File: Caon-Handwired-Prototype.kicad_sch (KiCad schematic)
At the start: 0 parts

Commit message: s
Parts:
- added S_C1: 0.1uF, Caon65:Capacitor_0805, symbol Device:C_Small
- added S_D1, S_D2, S_D3, S_D4, S_D5, S_D6, S_D7, S_D8: 1N4148, Caon65:D_SOD-123_1N4148W, symbol Caon65:Diode_1N4148W_SOD-123
- added U1: 74HC595, Caon65:74HC595A, symbol 74xx:74HC595
- added U2: Nice!Nano/SuperMini nRF52840, Caon65:SuperMini_NiceNano_USBdn, symbol Caon65:SuperMini/NiceNano_nRF52840
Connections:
- new net: S_D5.8 (A), U1.4 (QE)
- new net: S_D1.8 (A), U1.15 (QA)
- new net: S_D3.8 (A), U1.2 (QC)
- new net: S_D7.8 (A), U1.6 (QG)
- new net: S_D2.8 (A), U1.1 (QB)
- new net: S_D4.8 (A), U1.3 (QD)
- new net: S_D6.8 (A), U1.5 (QF)
- new net: S_D8.8 (A), U1.7 (QH)
- new net +3V3: S_C1.1, U1.10 (~{SRCLR}), U1.16 (VCC)
- new net CS: U1.12 (RCLK), U2.017 (P0.17)
- new net ENC1_A: U2.104 (P1.04-LF)
- new net ENC1_B: U2.106 (P1.06-LF)
- new net ENC2_A: U2.010 (P0.10-LF)
- new net ENC2_B: U2.009 (P0.09-LF)
- new net GND: S_C1.2, U1.13 (~{OE}), U1.8 (GND), U2.B- (BAT-), U2.GD (GND)
- new net MOSI: U1.14 (SER), U2.006 (P0.06)
- new net QH': U1.9 (QH')
- new net Row 0: U2.031 (P0.31-LF)
- new net Row 1: U2.029 (P0.29-LF)
- new net SCK: U1.11 (SRCLK), U2.008 (P0.08)
- new net VCC: U2.3V3
- new net col 0: S_D1.7 (K)
- new net col 1: S_D2.7 (K)
- new net col 2: S_D3.7 (K)
- new net col 3: S_D4.7 (K)
- new net col 4: S_D5.7 (K)
- new net col 5: S_D6.7 (K)
- new net col 6: S_D7.7 (K)
- new net col 7: S_D8.7 (K)
- no-connect marks 0 -> 15
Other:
- note added: "Nice!Nano/Super Mini"
- note added: "Shifter"

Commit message: Schematic Update
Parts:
- removed U2: Nice!Nano/SuperMini nRF52840, Caon65:SuperMini_NiceNano_USBdn, symbol Caon65:SuperMini/NiceNano_nRF52840
- added U2: SuperMini nRF52840, PCM_marbastlib-xp-promicroish:SuperMini_nRF52840_AH_USBup, symbol PCM_marbastlib-promicroish:SuperMini_nRF52840
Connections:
- net CS: now also U2.5 (P0.17)
- net ENC1_A: now also U2.11 (P1.04-LF)
- net ENC1_B: now also U2.12 (P1.06-LF)
- net ENC2_A: now also U2.23 (P0.10-LF)
- net ENC2_B: now also U2.24 (P0.09-LF)
- net GND: now also U2.14 (GND), U2.28 (GND), U2.3 (GND), U2.4 (GND)
- net MOSI: now also U2.1 (P0.06)
- net Row 0: now also U2.17 (P0.31-LF)
- net Row 1: now also U2.18 (P0.29-LF)
- net SCK: now also U2.2 (P0.08)
- net VCC: now also U2.16 (3V3)
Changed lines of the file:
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@@
-	)
-	(symbol
-		(lib_id "Caon65:SuperMini/NiceNano_nRF52840")
-		(at 63.5 50.8 0)
-		(unit 1)
-		(exclude_from_sim no)
-		(in_bom no)
-		(on_board yes)
-		(dnp no)
-		(fields_autoplaced yes)
-		(property "Reference" "U2"
-			(at 63.5 27.94 0)
-			(effects
-				(font
-					(size 1.27 1.27)
-				)
-				(hide yes)
-			)
-		)
-		(property "Value" "Nice!Nano/SuperMini nRF52840"
-			(at 63.5 29.21 0)
-			(effects
-				(font
-					(size 1.27 1.27)
-				)
-			)
-		)
-		(property "Footprint" "Caon65:SuperMini_NiceNano_USBdn"
-			(at 63.5 81.28 0)
-			(effects
-				(font
-					(size 1.27 1.27)
-				)
-				(hide yes)
-			)
-		)
-		(property "Datasheet" "https://wiki.icbbuy.com/doku.php?id=developmentboard:nrf52840"
-			(at 64.77 83.82 0)
-			(effects
-				(font
-					(size 1.27 1.27)
-				)
-				(hide yes)
-			)
-		)
-		(property "Description" "Symbol for an nicekeyboards nice!nano"
-			(at 63.5 50.8 0)
-			(effects
-				(font
-					(size 1.27 1.27)
-				)
-				(hide yes)
-			)
-		)
-		(property "Datasheet2" "https://nicekeyboards.com/docs/nice-nano/pinout-schematic"
-			(at 63.754 86.106 0)
-			(effects
-				(font
-					(size 1.27 1.27)
-				)
-				(hide yes)
-			)
-		)
-		(pin "006"
-		)
-		(pin "102"
-		)
-		(pin "106"
-		)
-		(pin "002"
-		)
-		(pin "017"
-		)
-		(pin "010"
-		)
-		(pin "GD"
-		)
-		(pin "RS"
-		)
-		(pin "008"
-		)
-		(pin "029"
-		)
-		(pin "022"
-		)
-		(pin "107"
-		)
-		(pin "009"
-		)
-		(pin "113"
-		)
-		(pin "100"
-		)
-		(pin "B+"
-		)
-		(pin "020"
-		)
-		(pin "104"
-		)
-		(pin "031"
-		)
-		(pin "101"
-		)
-		(pin "3V3"
-		)
-		(pin "024"
-		)
-		(pin "111"
-		)
-		(pin "115"
-		)
-		(pin "011"
-		)
-		(pin "B+"
-		)
-		(pin "B-"
-		)
-		(pin "GD"
-		)
-		(pin "GD"
-		)
-		(instances
-			(project "Caon-Handwired-Prototype"
-				(path "/8df2f29a-df03-4271-980f-9b5acafffeb5"
-					(reference "U2")
-					(unit 1)
-				)
-			)
-		)
 	)
 	(symbol
@@
 		(on_board yes)
 		(dnp no)
-		(property "Reference" "#PWR03"
+		(property "Reference" "#PWR02"
 			(at 95.25 46.99 0)
 			(effects
@@
 			(project "Caon-Handwired-Prototype"
 				(path "/8df2f29a-df03-4271-980f-9b5acafffeb5"
-					(reference "#PWR03")
+					(reference "#PWR02")
 					(unit 1)
 				)
@@
 		(on_board yes)
 		(dnp no)
-		(property "Reference" "#PWR04"
+		(property "Reference" "#PWR03"
 			(at 34.29 49.53 0)
 			(effects
@@
 			(project "Caon-Handwired-Prototype"
 				(path "/8df2f29a-df03-4271-980f-9b5acafffeb5"
-					(reference "#PWR04")
+					(reference "#PWR03")
 					(unit 1)
 				)
@@
 		(on_board yes)
 		(dnp no)
-		(property "Reference" "#PWR06"
+		(property "Reference" "#PWR04"
 			(at 129.54 74.93 0)
 			(effects
@@
 			(project "Caon-Handwired-Prototype"
 				(path "/8df2f29a-df03-4271-980f-9b5acafffeb5"
-					(reference "#PWR06")
-					(unit 1)
-				)
+					(reference "#PWR04")
+					(unit 1)
+				)
+			)
+		)
+	)
+	(symbol
+		(lib_id "PCM_marbastlib-promicroish:SuperMini_nRF52840")
+		(at 63.5 50.8 0)
+		(unit 1)
+		(exclude_from_sim no)
+		(in_bom no)
+		(on_board yes)
+		(dnp no)
+		(fields_autoplaced yes)
+		(property "Reference" "U2"
+			(at 63.5 26.67 0)
+			(effects
+				(font
+					(size 1.27 1.27)
+				)
+			)
+		)
+		(property "Value" "SuperMini nRF52840"
+			(at 63.5 29.21 0)
+			(effects
+				(font
+					(size 1.27 1.27)
+				)
+			)
+		)
+		(property "Footprint" "PCM_marbastlib-xp-promicroish:SuperMini_nRF52840_AH_USBup"
+			(at 63.5 81.28 0)
+			(effects
+				(font
+					(size 1.27 1.27)
+				)
+				(hide yes)
+			)
+		)
+		(property "Datasheet" "https://wiki.icbbuy.com/doku.php?id=developmentboard:nrf52840"
+			(at 64.77 83.82 0)
+			(effects
+				(font
+					(size 1.27 1.27)
+				)
+				(hide yes)
+			)
+		)
+		(property "Description" "Symbol for an nicekeyboards nice!nano"
+			(at 63.5 50.8 0)
+			(effects
+				(font
+					(size 1.27 1.27)
+				)
+				(hide yes)
+			)
+		)
+		(pin "3"
+		)
+		(pin "11"
+		)
+		(pin "15"
+		)
+		(pin "18"
+		)
+		(pin "19"
+		)
+		(pin "1"
+		)
+		(pin "2"
+		)
+		(pin "6"
+		)
+		(pin "5"
+		)
+		(pin "8"
+		)
+		(pin "7"
+		)
+		(pin "14"
+		)
+		(pin "17"
+		)
+		(pin "4"
+		)
+		(pin "9"
+		)
+		(pin "10"
+		)
+		(pin "12"
+		)
+		(pin "24"
+		)
+		(pin "26"
+		)
+		(pin "22"
+		)
+		(pin "20"
+		)
+		(pin "27"
+		)
+		(pin "13"
+		)
+		(pin "21"
+		)
+		(pin "29"
+		)
+		(pin "16"
+		)
+		(pin "23"
+		)
+		(pin "28"
+		)
+		(pin "25"
+		)
+		(instances
+			(project ""
+				(path "/8df2f29a-df03-4271-980f-9b5acafffeb5"
+					(reference "U2")
+					(unit 1)
+				)

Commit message: Schematic Update
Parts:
- S_C1: footprint Caon65:Capacitor_0805 -> Caon_Footprint:Capacitor_0805
- S_D1, S_D2, S_D3, S_D4, S_D5, S_D6, S_D7, S_D8: footprint Caon65:D_SOD-123_1N4148W -> Caon_Footprint:D_SOD-123_1N4148W
- U1: footprint Caon65:74HC595A -> Caon_Footprint:74HC595A
- U2: footprint PCM_marbastlib-xp-promicroish:SuperMini_nRF52840_AH_USBup -> Caon_Footprint:SuperMini_NiceNano_USBdn
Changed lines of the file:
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@@
 			)
 		)
-		(property "Footprint" "Caon65:D_SOD-123_1N4148W"
+		(property "Footprint" "Caon_Footprint:D_SOD-123_1N4148W"
 			(at 152.4 48.26 0)
 			(effects
@@
 			)
 		)
-		(property "Footprint" "Caon65:D_SOD-123_1N4148W"
+		(property "Footprint" "Caon_Footprint:D_SOD-123_1N4148W"
 			(at 152.4 38.1 0)
 			(effects
@@
 			)
 		)
-		(property "Footprint" "Caon65:D_SOD-123_1N4148W"
+		(property "Footprint" "Caon_Footprint:D_SOD-123_1N4148W"
 			(at 152.4 43.18 0)
 			(effects
@@
 			)
 		)
-		(property "Footprint" "Caon65:D_SOD-123_1N4148W"
+		(property "Footprint" "Caon_Footprint:D_SOD-123_1N4148W"
 			(at 152.4 53.34 0)
 			(effects
@@
 			)
 		)
-		(property "Footprint" "Caon65:74HC595A"
+		(property "Footprint" "Caon_Footprint:74HC595A"
 			(at 129.54 48.26 0)
 			(effects
@@
 			)
 		)
-		(property "Footprint" "Caon65:D_SOD-123_1N4148W"
+		(property "Footprint" "Caon_Footprint:D_SOD-123_1N4148W"
 			(at 143.51 50.8 0)
 			(effects
@@
 			)
 		)
-		(property "Footprint" "Caon65:D_SOD-123_1N4148W"
+		(property "Footprint" "Caon_Footprint:D_SOD-123_1N4148W"
 			(at 143.51 55.88 0)
 			(effects
@@
 			)
 		)
-		(property "Footprint" "Caon65:Capacitor_0805"
+		(property "Footprint" "Caon_Footprint:Capacitor_0805"
 			(at 110.49 49.53 0)
 			(effects
@@
 			)
 		)
-		(property "Footprint" "Caon65:D_SOD-123_1N4148W"
+		(property "Footprint" "Caon_Footprint:D_SOD-123_1N4148W"
 			(at 143.51 40.64 0)
 			(effects
@@
 			)
 		)
-		(property "Footprint" "Caon65:D_SOD-123_1N4148W"
+		(property "Footprint" "Caon_Footprint:D_SOD-123_1N4148W"
 			(at 143.51 45.72 0)
 			(effects
@@
 			)
 		)
-		(property "Footprint" "PCM_marbastlib-xp-promicroish:SuperMini_nRF52840_AH_USBup"
+		(property "Footprint" "Caon_Footprint:SuperMini_NiceNano_USBdn"
 			(at 63.5 81.28 0)
 			(effects

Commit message: Schematic update
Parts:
- removed S_D1, S_D2, S_D3, S_D4, S_D5, S_D6: 1N4148, Caon_Footprint:D_SOD-123_1N4148W, symbol Caon65:Diode_1N4148W_SOD-123
- renumbered S_D7 to S_D1, S_D8 to S_D2
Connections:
- no-connect marks 15 -> 21

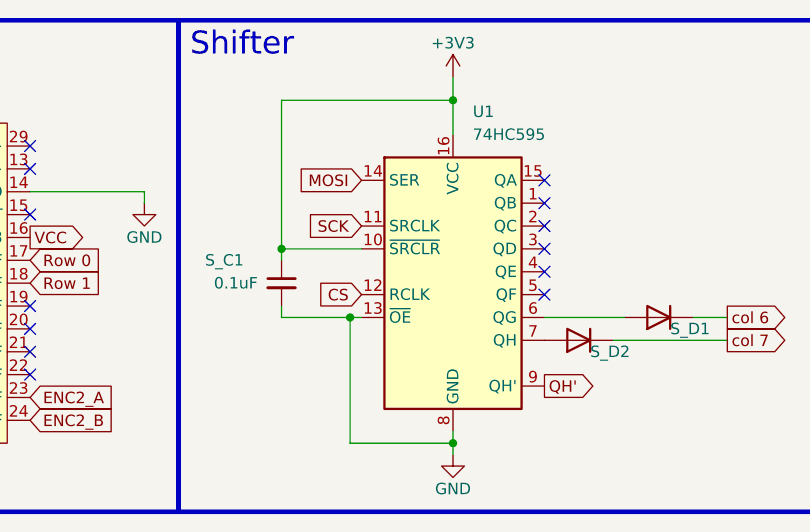
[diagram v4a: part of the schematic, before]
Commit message: Schematic and Footprint Update
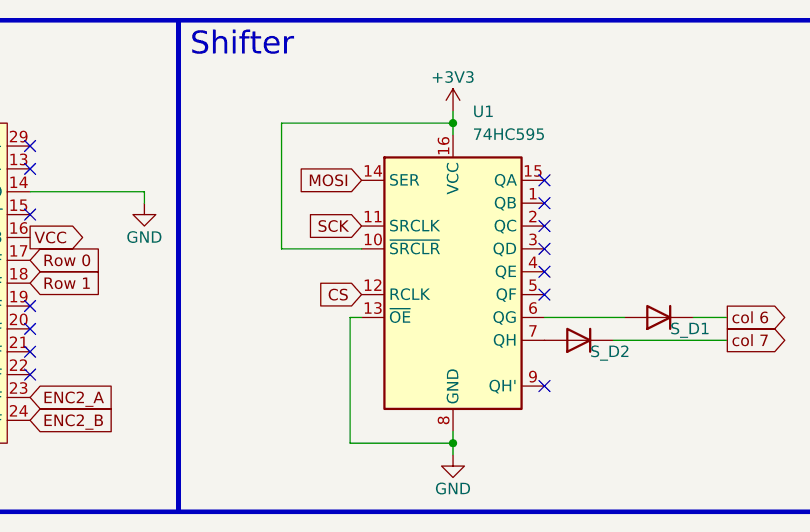
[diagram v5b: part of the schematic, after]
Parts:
- removed S_C1: 0.1uF, Caon_Footprint:Capacitor_0805, symbol Device:C_Small
- U1: footprint Caon_Footprint:74HC595A -> Package_DIP:DIP-16_W7.62mm
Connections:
- net QH': no longer names the net of U1.9 (QH')
- no-connect marks 21 -> 22
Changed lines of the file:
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@@
 	)
 	(junction
-		(at 110.49 45.72)
-		(diameter 0)
-		(color 0 0 0 0)
-	)
-	(junction
-		(at 118.11 53.34)
-		(diameter 0)
-		(color 0 0 0 0)
-	)
-	(junction
-		(at 129.54 29.21)
+		(at 129.54 31.75)
 		(diameter 0)
 		(color 0 0 0 0)
@@
 	)
 	(no_connect
+		(at 139.7 60.96)
+	)
+	(no_connect
 		(at 82.55 57.15)
 	)
@@
 	(wire
 		(pts
+			(xy 110.49 45.72) (xy 119.38 45.72)
+		)
+		(stroke
+			(width 0)
+			(type default)
+		)
+	)
+	(wire
+		(pts
+			(xy 129.54 31.75) (xy 129.54 33.02)
+		)
+		(stroke
+			(width 0)
+			(type default)
+		)
+	)
+	(wire
+		(pts
 			(xy 95.25 40.64) (xy 95.25 39.37)
 		)
@@
 	(wire
 		(pts
-			(xy 129.54 29.21) (xy 129.54 33.02)
-		)
-		(stroke
-			(width 0)
-			(type default)
-		)
-	)
-	(wire
-		(pts
 			(xy 82.55 39.37) (xy 95.25 39.37)
 		)
@@
 	(wire
 		(pts
-			(xy 129.54 26.67) (xy 129.54 29.21)
-		)
-		(stroke
-			(width 0)
-			(type default)
-		)
-	)
-	(wire
-		(pts
-			(xy 110.49 53.34) (xy 110.49 52.07)
+			(xy 129.54 30.48) (xy 129.54 31.75)
 		)
 		(stroke
@@
 	(wire
 		(pts
-			(xy 110.49 29.21) (xy 129.54 29.21)
+			(xy 110.49 31.75) (xy 129.54 31.75)
 		)
 		(stroke
@@
 	(wire
 		(pts
-			(xy 110.49 46.99) (xy 110.49 45.72)
-		)
-		(stroke
-			(width 0)
-			(type default)
-		)
-	)
-	(wire
-		(pts
 			(xy 118.11 53.34) (xy 118.11 67.31)
 		)
@@
 	(wire
 		(pts
-			(xy 118.11 53.34) (xy 110.49 53.34)
-		)
-		(stroke
-			(width 0)
-			(type default)
-		)
-	)
-	(wire
-		(pts
 			(xy 44.45 41.91) (xy 43.18 41.91)
 		)
@@
 	(wire
 		(pts
-			(xy 110.49 45.72) (xy 119.38 45.72)
-		)
-		(stroke
-			(width 0)
-			(type default)
-		)
-	)
-	(wire
-		(pts
-			(xy 110.49 45.72) (xy 110.49 29.21)
+			(xy 110.49 31.75) (xy 110.49 45.72)
 		)
 		(stroke
@@
 			(width 0)
 			(type default)
-		)
-	)
-	(global_label "QH'"
-		(shape output)
-		(at 139.7 60.96 0)
-		(fields_autoplaced yes)
-		(effects
-			(font
-				(size 1.27 1.27)
-			)
-			(justify left)
-		)
-		(property "Intersheetrefs" "${INTERSHEET_REFS}"
-			(at 145.951 60.96 0)
-			(effects
-				(font
-					(size 1.27 1.27)
-				)
-				(justify left)
-				(hide yes)
-			)
 		)
 	)
@@
 	(symbol
 		(lib_id "power:VCC")
-		(at 129.54 26.67 0)
+		(at 129.54 30.48 0)
 		(unit 1)
 		(exclude_from_sim no)
@@
 		(dnp no)
 		(property "Reference" "#PWR01"
+			(at 129.54 34.29 0)
+			(effects
+				(font
+					(size 1.27 1.27)
+				)
+				(hide yes)
+			)
+		)
+		(property "Value" "+3V3"
+			(at 129.54 26.67 0)
+			(effects
+				(font
+					(size 1.27 1.27)
+				)
+			)
+		)
+		(property "Footprint" ""
 			(at 129.54 30.48 0)
 			(effects
@@
 			)
 		)
-		(property "Value" "+3V3"
-			(at 129.54 22.86 0)
-			(effects
-				(font
-					(size 1.27 1.27)
-				)
-			)
-		)
-		(property "Footprint" ""
-			(at 129.54 26.67 0)
-			(effects
-				(font
-					(size 1.27 1.27)
-				)
-				(hide yes)
-			)
-		)
 		(property "Datasheet" ""
-			(at 129.54 26.67 0)
+			(at 129.54 30.48 0)
 			(effects
 				(font
@@
 		)
 		(property "Description" "Power symbol creates a global label with name \"VCC\""
-			(at 129.54 26.67 0)
+			(at 129.54 30.48 0)
 			(effects
 				(font
@@
 			)
 		)
-		(property "Footprint" "Caon_Footprint:74HC595A"
+		(property "Footprint" "Package_DIP:DIP-16_W7.62mm"
 			(at 129.54 48.26 0)
 			(effects
@@
 					(unit 1)
 				)
-			)
-		)
-	)
-	(symbol
-		(lib_id "Device:C_Small")
-		(at 110.49 49.53 0)
-		(unit 1)
-		(exclude_from_sim no)
-		(in_bom yes)
-		(on_board yes)
-		(dnp no)
-		(property "Reference" "S_C1"
-			(at 104.14 46.99 0)
-			(effects
-				(font
-					(size 1.27 1.27)
-				)
-			)
-		)
-		(property "Value" "0.1uF"
-			(at 105.41 49.53 0)
-			(effects
-				(font
-					(size 1.27 1.27)
-				)
-			)
-		)
-		(property "Footprint" "Caon_Footprint:Capacitor_0805"
-			(at 110.49 49.53 0)
-			(effects
-				(font
-					(size 1.27 1.27)
-				)
-				(hide yes)
-			)
-		)
-		(property "Datasheet" "~"
-			(at 110.49 49.53 0)
-			(effects
-				(font
-					(size 1.27 1.27)
-				)
-				(hide yes)
-			)
-		)
-		(property "Description" "Unpolarized capacitor, small symbol"
-			(at 110.49 49.53 0)
-			(effects
-				(font
-					(size 1.27 1.27)
-				)
-				(hide yes)
-			)
-		)
-		(pin "2"
-		)
-		(pin "1"
-		)
-		(instances
-			(project "Caon-Handwired-Prototype"
-				(path "/8df2f29a-df03-4271-980f-9b5acafffeb5"
-					(reference "S_C1")
-					(unit 1)
-				)

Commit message: Schematic, Footprint, PCB Update
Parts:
- S_D1, S_D2: footprint Caon_Footprint:D_SOD-123_1N4148W -> Diode_THT:D_DO-35_SOD27_P2.54mm_Vertical_AnodeUp
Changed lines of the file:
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@@
 			)
 		)
-		(property "Footprint" "Caon_Footprint:D_SOD-123_1N4148W"
+		(property "Footprint" "Diode_THT:D_DO-35_SOD27_P2.54mm_Vertical_AnodeUp"
 			(at 152.4 53.34 0)
 			(effects
@@
 			)
 		)
-		(property "Footprint" "Caon_Footprint:D_SOD-123_1N4148W"
+		(property "Footprint" "Diode_THT:D_DO-35_SOD27_P2.54mm_Vertical_AnodeUp"
 			(at 143.51 55.88 0)
 			(effects

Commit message: Update
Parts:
- removed S_D1, S_D2: 1N4148, Diode_THT:D_DO-35_SOD27_P2.54mm_Vertical_AnodeUp, symbol Caon65:Diode_1N4148W_SOD-123
- added ENC_R1, ENC_R2, ENC_R3, ENC_R4: 10k, Resistor_THT:R_Axial_DIN0204_L3.6mm_D1.6mm_P2.54mm_Vertical, symbol Device:R
- added SW1: EC11 ENCODER 1, PCM_marbastlib-various:ROT_Alps_EC11E-Switch, symbol Device:RotaryEncoder_Switch_MP
- added SW2: EC11 ENCODER 2, PCM_marbastlib-various:ROT_Alps_EC11E-Switch, symbol Device:RotaryEncoder_Switch_MP
- added S_D1, S_D2, S_D3, S_D4: ~, Caon_Footprint:D_DO-35_SOD27_P2.54mm_Caon65, symbol Diode:1N4148
- added U3: 74HC595, Package_DIP:DIP-16_W7.62mm, symbol 74xx:74HC595
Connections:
- net VCC is gone; now on net +3V3: U2.16 (3V3)
- net +3V3: now also ENC_R1.2, ENC_R2.2, ENC_R3.2, ENC_R4.2, U3.10 (~{SRCLR}), U3.16 (VCC)
- net CS: now also U3.12 (RCLK)
- net ENC1_A: now also ENC_R2.1, SW1.A
- net ENC1_B: now also ENC_R1.1, SW1.B
- net ENC2_A: now also ENC_R4.1, SW2.A
- net ENC2_B: now also ENC_R3.1, SW2.B
- net GND: now also SW1.C, SW1.MP, SW2.C, SW2.MP, U3.13 (~{OE}), U3.8 (GND)
- net MOSI: now also U3.14 (SER)
- net SCK: now also U3.11 (SRCLK)
- net at U1.6 (QG): now also S_D1.2 (A)
- net at U1.7 (QH): now also S_D2.2 (A)
- new net: S_D3.2 (A), U3.6 (QG)
- new net: S_D4.2 (A), U3.7 (QH)
- new net C1: S_D1.1 (K)
- new net C2: S_D2.1 (K)
- new net C3: S_D3.1 (K)
- new net C4: S_D4.1 (K)
- no-connect marks 22 -> 29
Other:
- note added: "Shifter0"
- note added: "Shifter1"
- note removed: "Shifter"
- moved on the sheet: U1

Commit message: Schematic update
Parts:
- removed SW2: EC11 ENCODER 2, PCM_marbastlib-various:ROT_Alps_EC11E-Switch, symbol Device:RotaryEncoder_Switch_MP
- added D1, D2, D3, D4, D5, D6, D7, D8: ~, Caon_Footprint:D_DO-35_SOD27_P2.54mm_Caon65, symbol Diode:1N4148
- added SW1, SW2, SW3, SW5, SW6, SW7: SW_PUSH_MX, Caon_Footprint:SW_PUSH_6mm, symbol Caon65:SW_PUSH_MX
- added SW8: EC11 ENCODER 1, PCM_marbastlib-various:ROT_Alps_EC11E-Switch, symbol Device:RotaryEncoder_Switch_MP
- renumbered SW1 to SW4, S_D3 to S_D2, S_D2 to S_D3, U3 to U2, U2 to U3
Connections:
- net ENC1_A is gone; now on net GND: ENC_R2.1, SW4.A, U3.11 (P1.04-LF)
- net C1: now also SW2.2, SW6.2
- net C2: now also SW3.2, SW7.2
- net C3: now also SW4.S2, SW8.S2
- net ENC2_A: now also SW8.A
- net ENC2_B: now also SW8.B
- net GND: now also SW8.C, SW8.MP
- net at SW4.S1: now also D7.2 (A)
- new net: D1.2 (A), SW1.1
- new net: D3.2 (A), SW3.1
- new net: D4.2 (A), SW5.1
- new net: D8.2 (A), SW8.S1
- new net: D5.2 (A), SW6.1
- new net: D2.2 (A), SW2.1
- new net: D6.2 (A), SW7.1
- new net C0: SW1.2, SW5.2
- new net R0: D1.1 (K), D2.1 (K), D3.1 (K), D7.1 (K)
- new net R1: D4.1 (K), D5.1 (K), D6.1 (K), D8.1 (K)
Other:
- note added: "Switch and Encoder Matrix"
- moved on the sheet: ENC_R1, ENC_R2, ENC_R3, ENC_R4, SW4
